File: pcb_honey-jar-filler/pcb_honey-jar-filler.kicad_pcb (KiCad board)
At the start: 2 copper layers, 160 x 100 mm, 96 parts, among them J1 12V, 5V, J10 OLED_3v3, GND, J11 OLED_SDA, SCL, J12 MOS out (COM, Drain), J13 230V Heater, J14 3V3, J15 12V, 5V, J16 LED2, J17 GND, J18 GND, J19 Servo, J2 12V, J20 Conn_01x07_Pin, J21 LED1, J24 load-cell (red, black), J25 load-cell (white, green), J26 B+ B- (free), J27 Supply, J28 Relay fallback, J3 3V3, J4 button1, button2, J5 4...7V, J6 Encoder A, B, J7 Encoder Button, Pos-sw, J8 MOS out (COM, Drain), K6 Relay_LEG-xxF, K7 Relay_LEG-xxF, M2 DC-worm-gear motor (Carousell), Q1 IRLB8721PBF, Q2 IRLB8721PBF, Q6 IRF5305, U1 esp32-devkit-v1_30Pin, U10 LM2576T-ADJ, U3 ULN2003, U4 HX711_24-bit-ADC_weight-scale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, U9 LM2576T-5

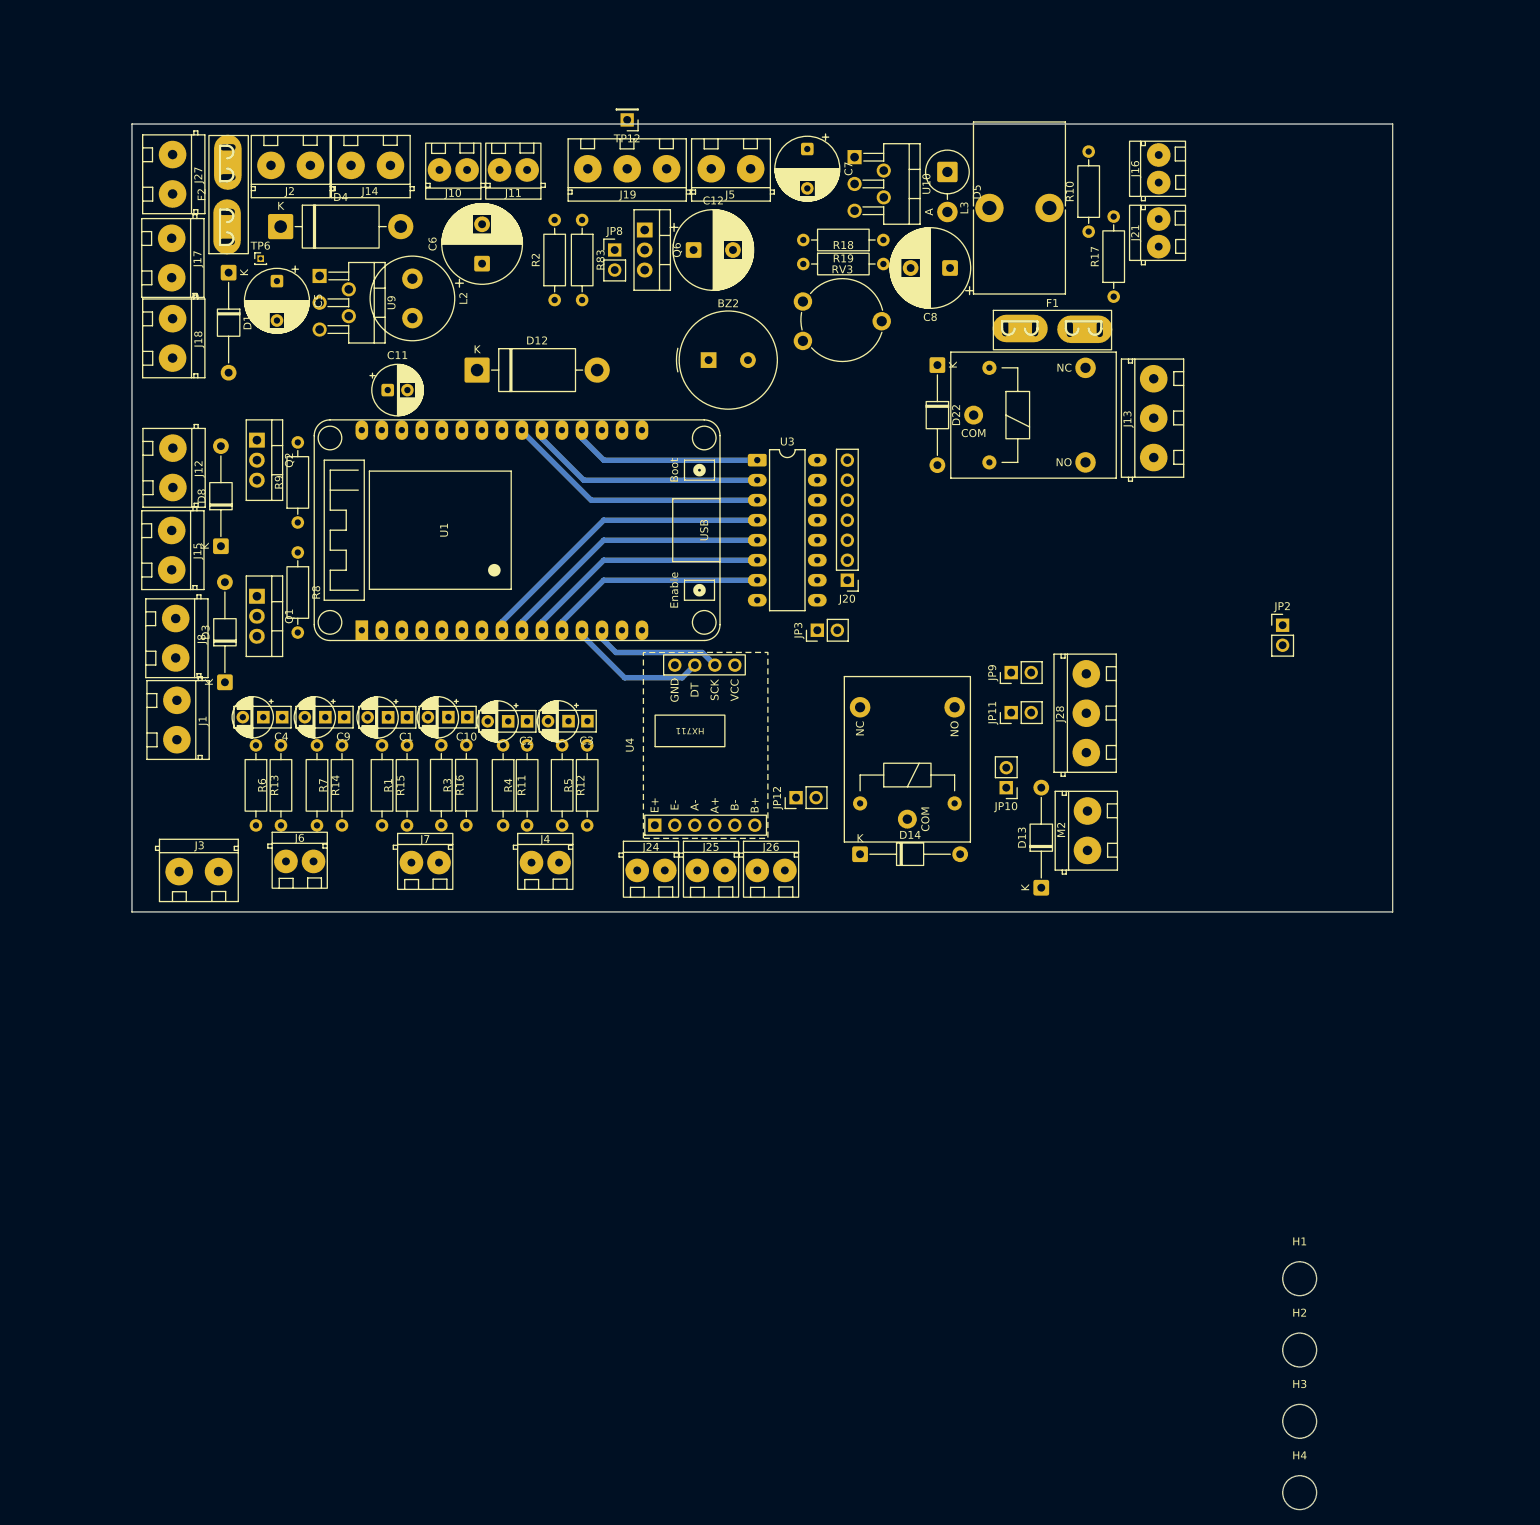
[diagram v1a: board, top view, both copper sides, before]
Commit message: pcb: initial routing complete, some terminals -> JST connector
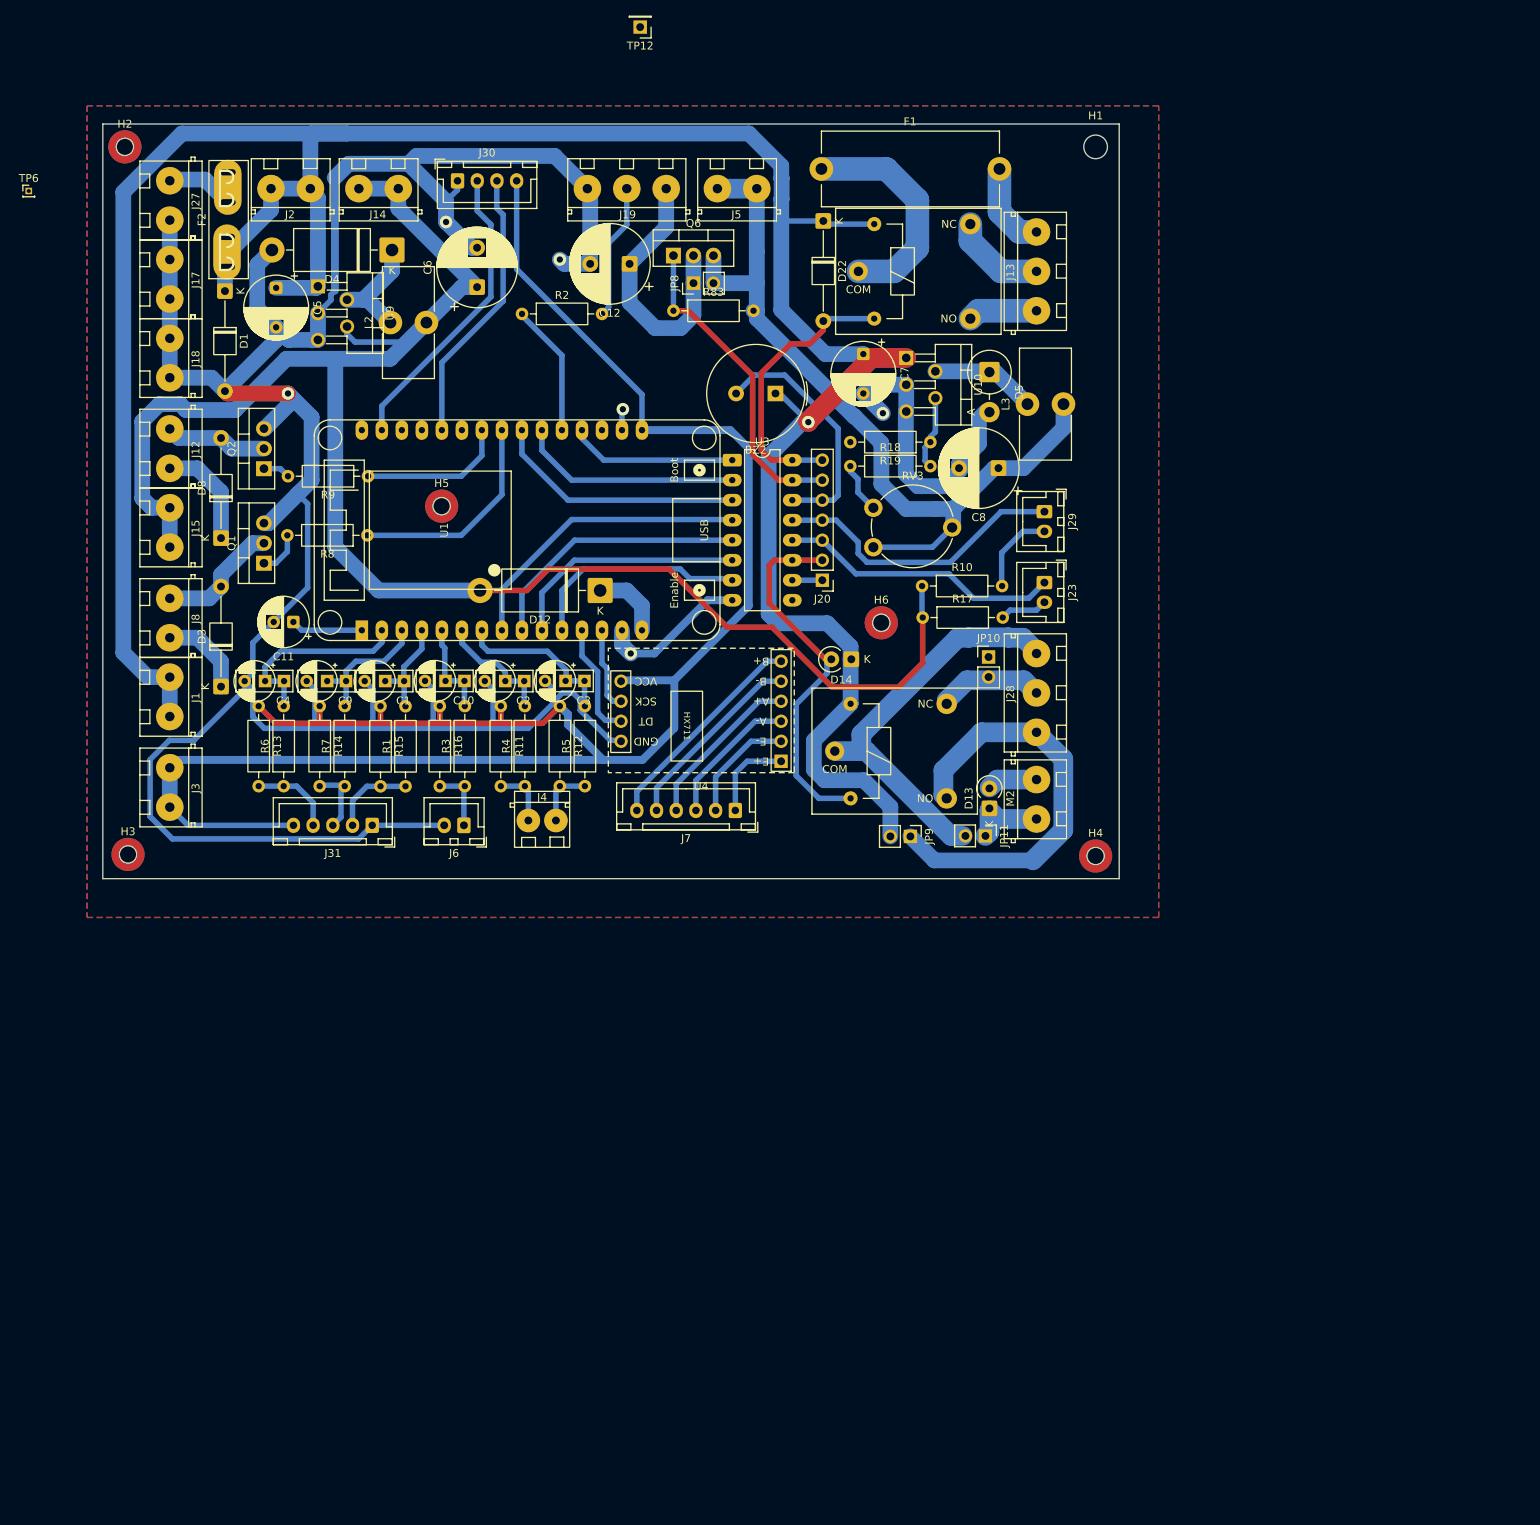
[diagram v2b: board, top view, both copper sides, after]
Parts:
- removed J10: OLED_3v3, GND, terminals_libJonny:ScrewTerminal_P3.5mm_2Pin_FP7x7
- removed J11: OLED_SDA, SCL, terminals_libJonny:ScrewTerminal_P3.5mm_2Pin_FP7x7
- removed J16: LED2, terminals_libJonny:ScrewTerminal_P3.5mm_2Pin_FP7x7
- removed J21: LED1, terminals_libJonny:ScrewTerminal_P3.5mm_2Pin_FP7x7
- removed J24: load-cell (red, black), terminals_libJonny:ScrewTerminal_P3.5mm_2Pin_FP7x7
- removed J25: load-cell (white, green), terminals_libJonny:ScrewTerminal_P3.5mm_2Pin_FP7x7
- removed J26: B+ B- (free), terminals_libJonny:ScrewTerminal_P3.5mm_2Pin_FP7x7
- removed JP12, JP2: Jumper_2_Bridged, Connector_PinHeader_2.54mm:PinHeader_1x02_P2.54mm_Vertical
- removed JP3: Jumper_2_Open, Connector_PinHeader_2.54mm:PinHeader_1x02_P2.54mm_Vertical
- added H5: MountingHole_Pad, mountingHoles_libJonny:MountingHole_2.2mm_NPTH-with-pad_DRC-clearance-error, F.Cu at (59.0, 66.8)
- added H6: MountingHole_Pad, mountingHoles_libJonny:MountingHole_2.2mm_NPTH-with-pad_DRC-clearance-error, F.Cu at (114.8, 81.6)
- added J23: Conn_01x02_Pin, Connector_JST:JST_XH_B2B-XH-A_1x02_P2.50mm_Vertical, F.Cu at (135.5, 76.5)
- added J29: Conn_01x02_Pin, Connector_JST:JST_XH_B2B-XH-A_1x02_P2.50mm_Vertical, F.Cu at (135.5, 67.5)
- added J30: Conn_01x04_Pin, Connector_JST:JST_XH_B4B-XH-A_1x04_P2.50mm_Vertical, F.Cu at (61.0, 25.5)
- added J31: Conn_01x05_Pin, Connector_JST:JST_XH_B5B-XH-A_1x05_P2.50mm_Vertical, F.Cu at (50.2, 107.3)
- D13, D14: footprint Diode_THT:D_T-1_P12.70mm_Horizontal -> Diode_THT:D_T-1_P2.54mm_Vertical_KathodeUp
- F1: footprint misc_libJonny:Fuseholder_Automotive-Mini_Fuse11x4x16_Footprint15x5_Inline -> Fuse:Fuseholder_Cylinder-5x20mm_Stelvio-Kontek_PTF78_Horizontal_Open
- H1: footprint MountingHole:MountingHole_4.3mm_M4_DIN965 -> MountingHole:MountingHole_3mm
- H2, H3, H4: value MountingHole -> MountingHole_Pad; footprint MountingHole:MountingHole_4.3mm_M4_DIN965 -> mountingHoles_libJonny:MountingHole_2.2mm_NPTH-with-pad_DRC-clearance-error
- J1: value 12V, 5V -> 12V
- J15: value 12V, 5V -> 5V
- J4: value button1, button2 -> reserve Buttons
- J6: value Encoder A, B -> Conn_01x02_Pin; footprint terminals_libJonny:ScrewTerminal_P3.5mm_2Pin_FP7x7 -> Connector_JST:JST_XH_B2B-XH-A_1x02_P2.50mm_Vertical
- J7: value Encoder Button, Pos-sw -> Conn_01x06_Pin; footprint terminals_libJonny:ScrewTerminal_P3.5mm_2Pin_FP7x7 -> Connector_JST:JST_XH_B6B-XH-A_1x06_P2.50mm_Vertical
- L2: value 330u -> 100u; footprint Inductor_THT:L_Radial_D10.5mm_P5.00mm_Abacron_AISR-01 -> Inductor_THT:L_Toroid_Vertical_L14.0mm_W6.3mm_P4.57mm_Pulse_A
- L3: footprint Inductor_THT:L_Toroid_Vertical_L21.6mm_W11.4mm_P7.62mm_Pulse_KM-3 -> Inductor_THT:L_Toroid_Vertical_L14.0mm_W6.3mm_P4.57mm_Pulse_A
- moved H2 213.4 mm to (18.8, 21.2)
- moved H3 165.2 mm to (19.2, 111.0)
- moved H1 146.0 mm to (142.0, 21.2)
- moved H4 84.8 mm to (142.0, 111.2)
- moved R10 49.7 mm to (120.0, 76.9), turned to 0 degrees
- moved R17 47.4 mm to (120.1, 80.9), turned to 0 degrees
- moved J7 41.6 mm to (96.3, 105.4), turned to 180 degrees
- moved D12 32.0 mm to (79.1, 77.5), turned to 180 degrees
- moved C11 31.8 mm to (40.2, 81.5), turned to 180 degrees
- moved F1 31.0 mm to (107.2, 24.0)
- moved TP6 30.7 mm to (6.60, 26.8)
- moved RV3 27.7 mm to (113.8, 72.0)
- moved C7 27.0 mm to (112.5, 47.5)
- moved R18 26.3 mm to (110.9, 61.7)
- moved R19 26.3 mm to (121.0, 58.7)
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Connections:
- C5 pad 1: +24V filtered -> +12V
- C7 pad 1: +24V filtered -> +12V
- D14 pad 2: Net-(D14-A) -> /OD_Relay-motor
- D22 pad 2: Net-(D22-A) -> /OD_Relay-heater
- F1 pad 2: Net-(J13-Pin_2) -> Net-(J13-Pin_3)
- J1 pad 1: +5V -> +12V
- J15 pad 2: +12V -> +5V
- J20 pad 3: /OD_Relay-heater -> /OD_LED1
- J20 pad 4: /OD_LED1 -> /OD_LED2
- J20 pad 5: /OD_LED2 -> /OD_Buzzer
- J20 pad 6: /OD_Buzzer -> /OD_EN-Servo-pwr
- J20 pad 7: /OD_EN-Servo-pwr -> /OD_Relay-heater
- J6 pad 1: /Digital-Input-Filter2/switch-terminal -> /Pos-SW
- J6 pad 2: /Digital-Input-Filter3/switch-terminal -> GND
- J7 pad 1: /Digital-Input-Filter4/switch-terminal -> Net-(J7-Pin_1)
- J7 pad 2: /Digital-Input-Filter5/switch-terminal -> Net-(J7-Pin_2)
- JP10 pad 2: Net-(J28-Pin_1) -> Net-(J28-Pin_2)
- JP11 pad 2: Net-(J28-Pin_2) -> Net-(J28-Pin_3)
- JP9 pad 1: Net-(J28-Pin_3) -> Net-(J28-Pin_1)
- K6 pad 12: Net-(J13-Pin_1) -> Net-(J13-Pin_2)
- K6 pad 14: Net-(J13-Pin_3) -> Net-(J13-Pin_1)
- K6 pad A2: Net-(D22-A) -> /OD_Relay-heater
- K7 pad 11: Net-(J28-Pin_2) -> Net-(J28-Pin_3)
- K7 pad 12: Net-(J28-Pin_1) -> Net-(J28-Pin_2)
- K7 pad 14: Net-(J28-Pin_3) -> Net-(J28-Pin_1)
- K7 pad A2: Net-(D14-A) -> /OD_Relay-motor
- R1 pad 1: /Digital-Input-Filter4/switch-terminal -> /Encoder-btn
- R13 pad 2: /Digital-Input-Filter2/switch-terminal -> /Encoder-A
- R14 pad 2: /Digital-Input-Filter3/switch-terminal -> /Encoder-B
- R15 pad 2: /Digital-Input-Filter4/switch-terminal -> /Encoder-btn
- R16 pad 2: /Digital-Input-Filter5/switch-terminal -> /Pos-SW
- R3 pad 1: /Digital-Input-Filter5/switch-terminal -> /Pos-SW
- R6 pad 1: /Digital-Input-Filter2/switch-terminal -> /Encoder-A
- R7 pad 1: /Digital-Input-Filter3/switch-terminal -> /Encoder-B
- U1 pad 19: /GPIO_EN-Servo-pwr -> /GPIO_Relay-heater
- U1 pad 21: /GPIO_Buzzer -> /GPIO_EN-Servo-pwr
- U1 pad 22: /GPIO_LED2 -> /GPIO_Buzzer
- U1 pad 23: /GPIO_MOS-reserve -> /GPIO_MOS-valve
- U1 pad 24: /GPIO_MOS-valve -> /GPIO_MOS-reserve
- U1 pad 8: /GPIO_LED1 -> /GPIO_LED2
- U1 pad 9: /GPIO_Relay-heater -> /GPIO_LED1
- U10 pad 1: +24V filtered -> +12V
- U3 pad 1: /GPIO_EN-Servo-pwr -> /GPIO_Relay-heater
- U3 pad 12: /OD_Relay-heater -> /OD_LED1
- U3 pad 13: /OD_LED1 -> /OD_LED2
- U3 pad 14: /OD_LED2 -> /OD_Buzzer
- U3 pad 15: /OD_Buzzer -> /OD_EN-Servo-pwr
- U3 pad 16: /OD_EN-Servo-pwr -> /OD_Relay-heater
- U3 pad 2: /GPIO_Buzzer -> /GPIO_EN-Servo-pwr
- U3 pad 3: /GPIO_LED2 -> /GPIO_Buzzer
- U3 pad 4: /GPIO_LED1 -> /GPIO_LED2
- U3 pad 5: /GPIO_Relay-heater -> /GPIO_LED1
- U4 pad 1: Net-(J24-Pin_2) -> Net-(J7-Pin_1)
- U4 pad 2: Net-(J24-Pin_1) -> Net-(J7-Pin_2)
- U4 pad 3: Net-(J25-Pin_1) -> Net-(J7-Pin_3)
- U4 pad 4: Net-(J25-Pin_2) -> Net-(J7-Pin_4)
- U4 pad 5: Net-(J26-Pin_1) -> Net-(J7-Pin_5)
- U4 pad 6: Net-(J26-Pin_2) -> Net-(J7-Pin_6)
- U9 pad 1: +24V filtered -> +12V
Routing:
- net GND: track 0.00 -> 421.9 mm, vias 0 -> 6
- net +12V: track 0.00 -> 351.4 mm, vias 0 -> 1
- net +3V3: track 0.00 -> 244.7 mm
- net +5V: track 0.00 -> 222.4 mm
- net 4...7V: track 0.00 -> 103.7 mm
- net Net-(J28-Pin_1): track 0.00 -> 53.6 mm
- net Net-(J28-Pin_3): track 0.00 -> 51.2 mm
- net /OD_Relay-motor: track 0.00 -> 47.3 mm
- net /OD_EN-Servo-pwr: track 0.00 -> 41.1 mm
- net /I2C-SCL_OLED: track 0.00 -> 38.1 mm
- net /OD_LED2: track 0.00 -> 37.7 mm
- net /OD_Relay-heater: track 0.00 -> 35.9 mm
- net /OD_LED1: track 0.00 -> 35.9 mm
- net /I2C-SDA_OLED: track 0.00 -> 35.2 mm
- net Net-(J19-Pin_1): track 0.00 -> 34.1 mm
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- added copper zone on B.Cu, net GND
- added copper zone on F.Cu, net GND
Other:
- board size 160 x 100 mm -> 129 x 95.8 mm
